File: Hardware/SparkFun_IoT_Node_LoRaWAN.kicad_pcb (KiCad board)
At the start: 4 copper layers, 59 x 79.5 mm, 234 parts, among them J1 USB_C_Receptacle, J10 microSD_Friction, J11 Qwiic_RA, J2 Conn_01x03, J3 USB_C_Receptacle, J4 SWD, J5 Conn_01x10, J6 Conn_01x10, J7 Conn_01x10, J8 Conn_01x10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

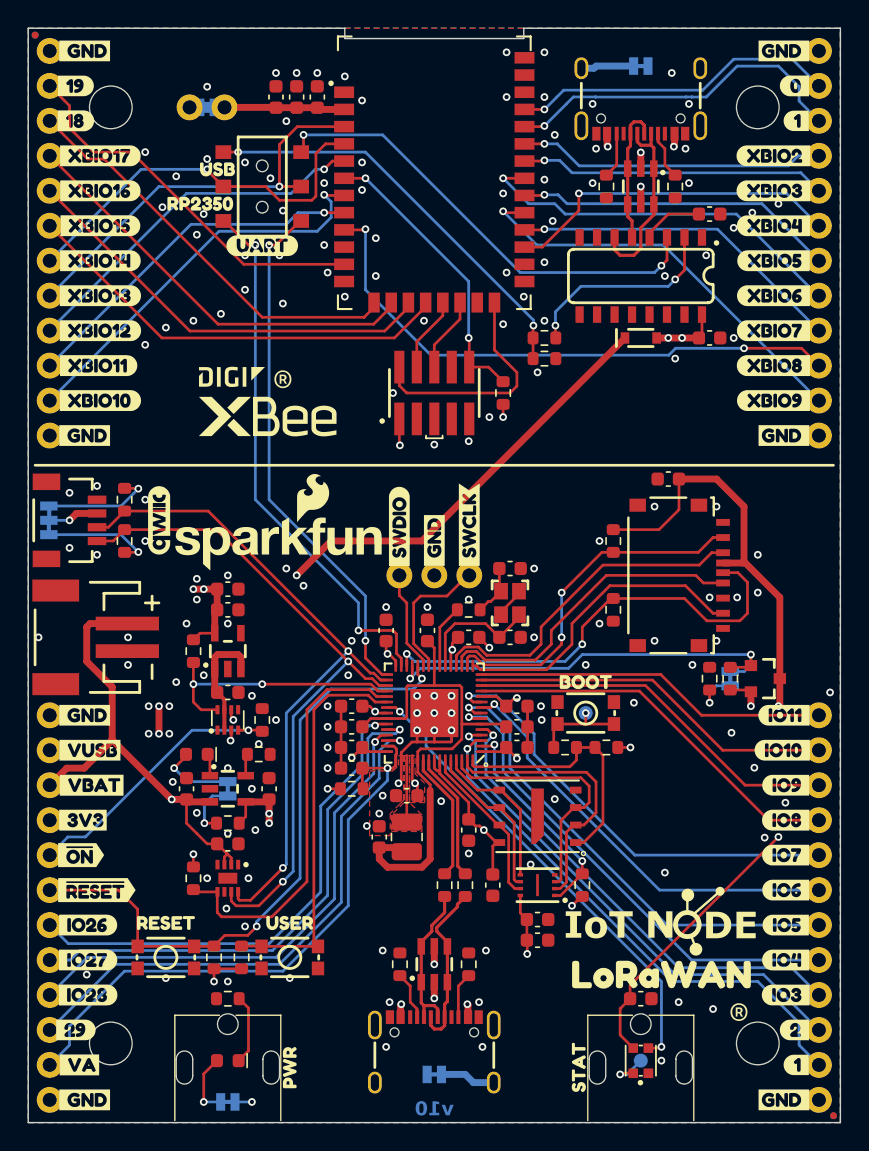
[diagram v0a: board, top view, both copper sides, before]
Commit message: Design review updates
Fix layers to standard SFE usage
Add link to enclosure and PDF of dimensions
Move fiducials away from PTH pads
Add USB test points
Add XBLR debug test points
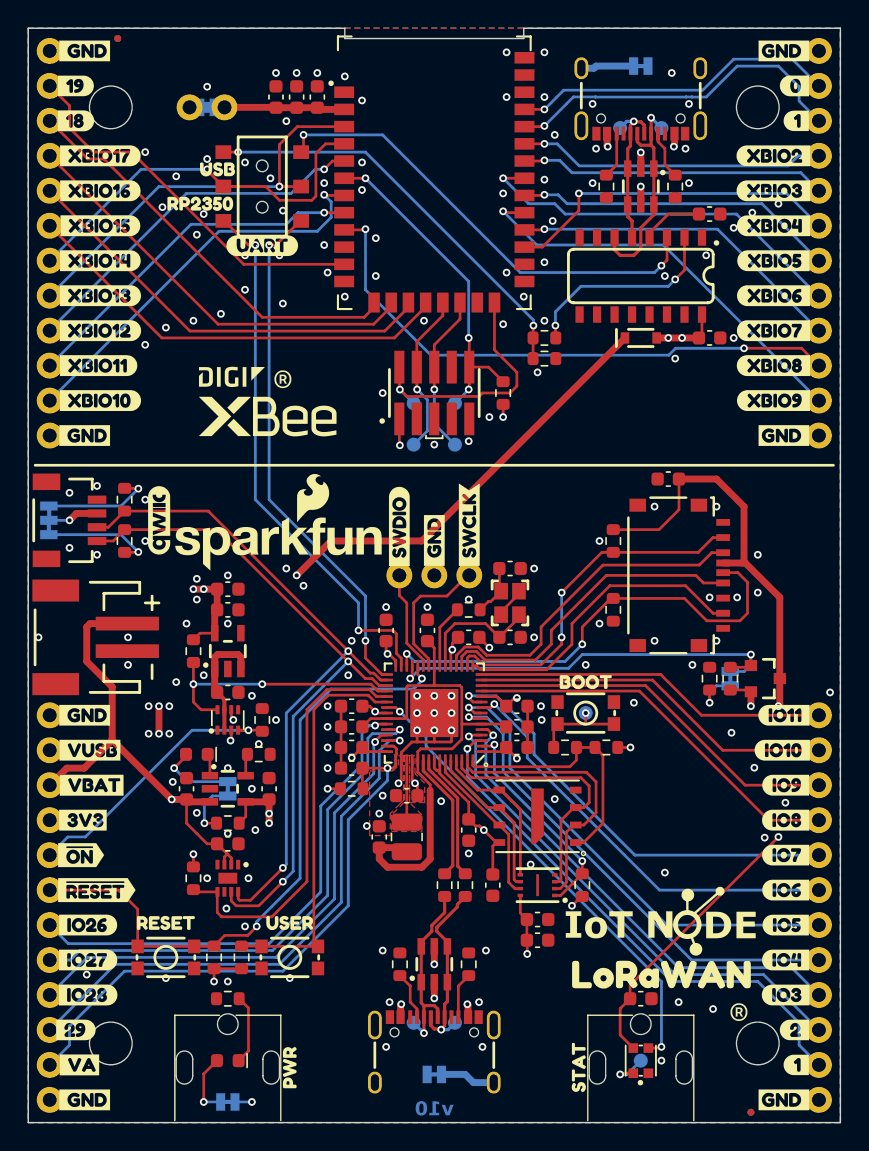
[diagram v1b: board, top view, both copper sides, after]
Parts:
- removed G3: OSHW_Logo, SparkFun-Aesthetic:Creative_Commons_License
- added TP10: 1.0mm, SparkFun-Connector:TestPoint-1.0mm, B.Cu at (113.5, 67.5)
- added TP3: 1.0mm, SparkFun-Connector:TestPoint-1.0mm, B.Cu at (98.5, 132.5)
- added TP4: 1.0mm, SparkFun-Connector:TestPoint-1.0mm, B.Cu at (101.5, 132.5)
- added TP5: 1.0mm, SparkFun-Connector:TestPoint-1.0mm, B.Cu at (101.5, 90.5)
- added TP6: 1.0mm, SparkFun-Connector:TestPoint-1.0mm, B.Cu at (98.5, 90.5)
- added TP7: 1.0mm, SparkFun-Connector:TestPoint-1.0mm, B.Cu at (98.5, 87.5)
- added TP8: 1.0mm, SparkFun-Connector:TestPoint-1.0mm, B.Cu at (101.5, 87.5)
- added TP9: 1.0mm, SparkFun-Connector:TestPoint-1.0mm, B.Cu at (116.5, 67.5)
- moved FID1 6.01 mm to (77.0, 61.0)
- moved FID2 6.01 mm to (123.0, 139.0)
- moved FID3 6.01 mm to (77.0, 61.0)
- moved FID4 6.01 mm to (123.0, 139.0)
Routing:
- net XBLR_SWCLK: track 5.47 -> 11.8 mm, vias 0 -> 1
- net XBLR_SWO: track 5.46 -> 11.7 mm, vias 0 -> 1
- net XBLR_~{RESET}: track 21.3 -> 24.4 mm, vias 2 -> 3
- net XBLR_USB_D-: track 13.7 -> 15.9 mm, vias 0 -> 1
- net /USB_D-: track 11.2 -> 13.5 mm, vias 0 -> 1
- net XBLR_SWDIO: track 17.1 -> 18.8 mm, vias 0 -> 1
- net /USB_D+: track 12.5 -> 13.8 mm, vias 0 -> 1
- net XBLR_USB_D+: track 10.2 -> 11.4 mm, vias 0 -> 1
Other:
- board text added: "Enclosure: https://www.hammfg.com/part/1555EF17GY?referer=529 https://www.hammfg.com/files/parts/pdf/1555EF17GY.pdf?v=1697661937"
- board text removed: "Released under the Creative Commons Attribution Share-Alike 4.0 License"
- board text removed: "https://creativecommons.org/licenses/by-sa/4.0/"

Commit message: Add XBLR 3D model
Also fix RP2350A library reference
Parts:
- U1: footprint SparkFun_IoT_Node_LoRaWAN:RP2350A -> SparkFun-Semiconductor-Standard:QFN-60-1EP_7x7mm_P0.4mm_EP3.5x3.5mm
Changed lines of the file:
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@@
 		)
 	)
-	(footprint "SparkFun_IoT_Node_LoRaWAN:RP2350A"
+	(footprint "SparkFun-Semiconductor-Standard:QFN-60-1EP_7x7mm_P0.4mm_EP3.5x3.5mm"
 		(layer "F.Cu")
 		(at 100 110 180)
@@
 			)
 		)
-		(property "Footprint" "SparkFun_IoT_Node_LoRaWAN:RP2350A"
+		(property "Footprint" "SparkFun-Semiconductor-Standard:QFN-60-1EP_7x7mm_P0.4mm_EP3.5x3.5mm"
 			(at 0 0 180)
 			(unlocked yes)
@@
 			)
 		)
-		(property "Datasheet" ""
-			(at 0 0 180)
+		(property "Datasheet" "https://datasheets.raspberrypi.com/rp2350/rp2350-datasheet.pdf"
+			(at 0 5.5 180)
 			(unlocked yes)
 			(layer "F.Fab")
@@
 			(thermal_bridge_angle 0)
 		)
-		(pad "EPAD" smd rect
+		(pad "EP" smd rect
 			(at 0 0 180)
 			(size 3.5 3.5)
@@
 			(thermal_bridge_angle 0)
 		)
+		(model "${SPARKFUN_KICAD_LIBRARY}/Footprints/SparkFun-3D-models/Semiconductor-Standard/QFN-60-1EP_7x7mm_P0.4mm_EP3.5x3.5mm.step"
+			(offset
+				(xyz 0 0 0)
+			)
+			(scale
+				(xyz 1 1 1)
+			)
+			(rotate
+				(xyz 0 0 0)
+			)
+		)
 	)
 	(footprint "SparkFun-Resistor:R_0603_1608Metric"
@@
 		(fp_arc
 			(start 1.5653 -5.257777)
-			(mid 1.834722 -5.146216)
+			(mid 1.834725 -5.146217)
 			(end 1.9463 -4.8768)
 			(stroke
@@
 			)
 		)
+		(model "${KIPRJMOD}/SparkFun_IoT_Node_LoRaWAN_3D_Models/XBLR_UFL.step"
+			(offset
+				(xyz -6.77 -9.65 0.8)
+			)
+			(scale
+				(xyz 1 1 1)
+			)
+			(rotate
+				(xyz 0 0 0)
+			)
+		)

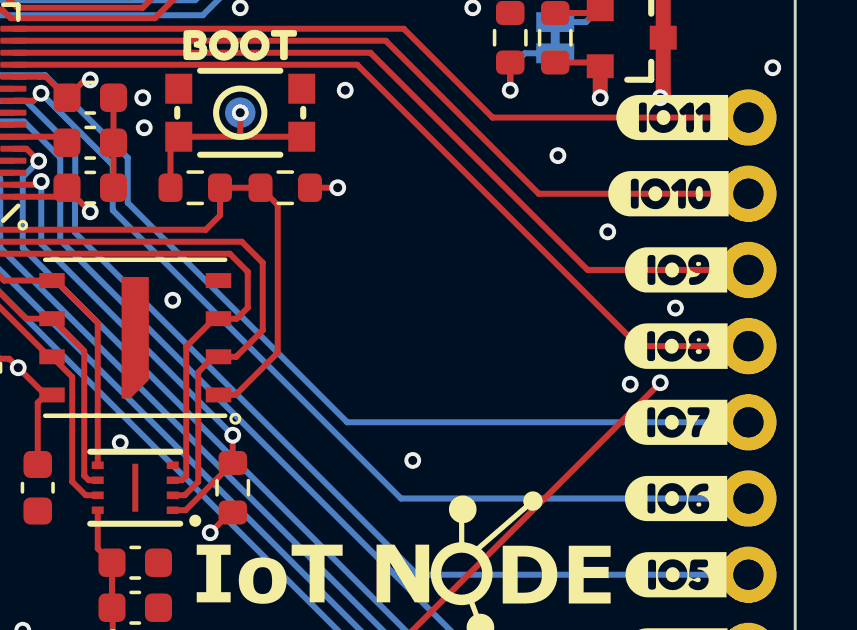
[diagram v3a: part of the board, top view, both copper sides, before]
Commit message: Add OSHW logo to silkscreen
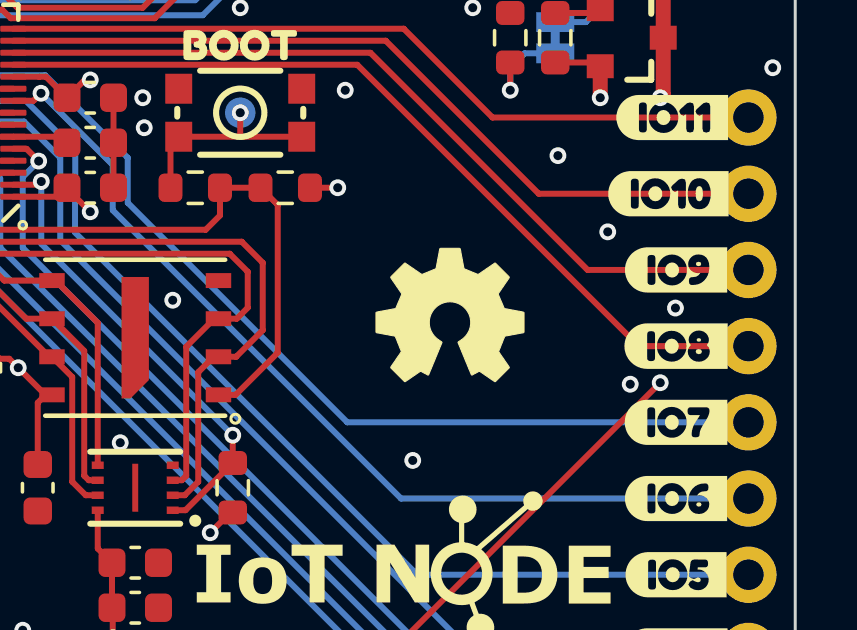
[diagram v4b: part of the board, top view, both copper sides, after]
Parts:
- added Ref**: Val**, SparkFun-Aesthetic:OSHW_Logo_5mm, F.Cu at (118.0, 117.0)
